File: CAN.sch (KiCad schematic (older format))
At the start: 2 parts

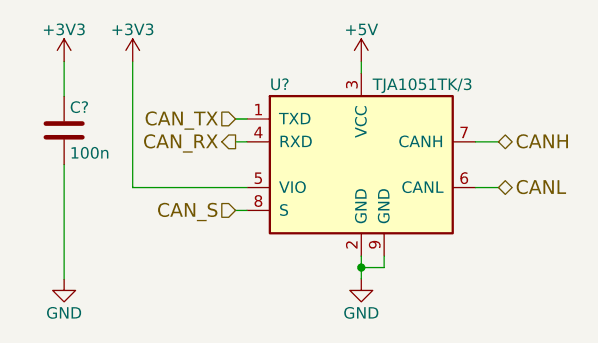
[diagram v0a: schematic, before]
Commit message: Finished schematic
Motordriver still needs footprint, it's necessary to choose new bulk capacitors
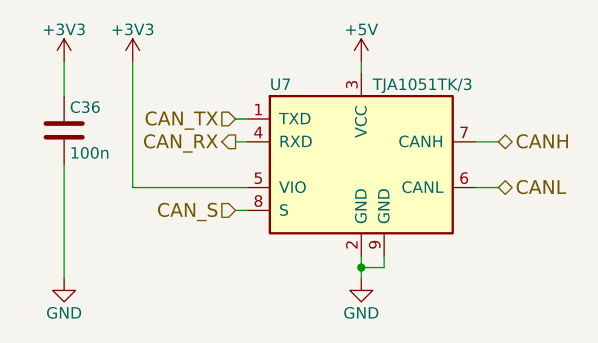
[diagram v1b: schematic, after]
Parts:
- C36: renamed from C?; footprint (none) -> Capacitors_SMD:C_0402
- gave numbers to parts that had none: 1
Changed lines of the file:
@@
 $EndDescr
 $Comp
-L TJA1051TK/3 U?
+L TJA1051TK/3 U7
 U 1 1 5A0B0C6C
 P 5900 4000
-F 0 "U?" H 5500 4350 50  0000 L CNN
+F 0 "U7" H 5500 4350 50  0000 L CNN
 F 1 "TJA1051TK/3" H 5950 4350 50  0000 L CNN
 F 2 "Housings_DFN_QFN:DFN-8-1EP_3x3mm_Pitch0.65mm" H 5900 3500 50  0001 C CIN
@@
 	5900 3550 5900 3600
 $Comp
-L GND #PWR?
+L GND #PWR85
 U 1 1 5A0B0CD3
 P 5900 4500
-F 0 "#PWR?" H 5900 4250 50  0001 C CNN
+F 0 "#PWR85" H 5900 4250 50  0001 C CNN
 F 1 "GND" H 5900 4350 50  0000 C CNN
 F 2 "" H 5900 4500 50  0001 C CNN
@@
 $EndComp
 Wire Wire Line
-	5900 4400 5900 4450
-Wire Wire Line
-	5900 4450 5900 4500
+	5900 4400 5900 4500
 Wire Wire Line
 	6000 4400 6000 4450
@@
 Connection ~ 5900 4450
 $Comp
-L +3V3 #PWR?
+L +3V3 #PWR83
 U 1 1 5A0B0CFF
 P 4900 3550
-F 0 "#PWR?" H 4900 3400 50  0001 C CNN
+F 0 "#PWR83" H 4900 3400 50  0001 C CNN
 F 1 "+3V3" H 4900 3690 50  0000 C CNN
 F 2 "" H 4900 3550 50  0001 C CNN
@@
 	5350 3800 5400 3800
 $Comp
-L C C?
+L C C36
 U 1 1 5A0B0D90
 P 4600 3850
-F 0 "C?" H 4625 3950 50  0000 L CNN
+F 0 "C36" H 4625 3950 50  0000 L CNN
 F 1 "100n" H 4625 3750 50  0000 L CNN
-F 2 "" H 4638 3700 50  0001 C CNN
+F 2 "Capacitors_SMD:C_0402" H 4638 3700 50  0001 C CNN
 F 3 "" H 4600 3850 50  0001 C CNN
 	1    4600 3850
@@
 $EndComp
 $Comp
-L +3V3 #PWR?
+L +3V3 #PWR81
 U 1 1 5A0B0DF3
 P 4600 3550
-F 0 "#PWR?" H 4600 3400 50  0001 C CNN
+F 0 "#PWR81" H 4600 3400 50  0001 C CNN
 F 1 "+3V3" H 4600 3690 50  0000 C CNN
 F 2 "" H 4600 3550 50  0001 C CNN
@@
 $EndComp
 $Comp
-L GND #PWR?
+L GND #PWR82
 U 1 1 5A0B0E04
 P 4600 4500
-F 0 "#PWR?" H 4600 4250 50  0001 C CNN
+F 0 "#PWR82" H 4600 4250 50  0001 C CNN
 F 1 "GND" H 4600 4350 50  0000 C CNN
 F 2 "" H 4600 4500 50  0001 C CNN
@@
 	4600 3550 4600 3700
 $Comp
-L +5V #PWR?
+L +5V #PWR84
 U 1 1 5A0B0E45
 P 5900 3550
-F 0 "#PWR?" H 5900 3400 50  0001 C CNN
+F 0 "#PWR84" H 5900 3400 50  0001 C CNN
 F 1 "+5V" H 5900 3690 50  0000 C CNN
 F 2 "" H 5900 3550 50  0001 C CNN

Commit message: udated schematics
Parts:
- C36: value 100n -> 100n 6V3
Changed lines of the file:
@@
 	5900 3550 5900 3600
 $Comp
-L GND #PWR087
+L GND #PWR89
 U 1 1 5A0B0CD3
 P 5900 4500
-F 0 "#PWR087" H 5900 4250 50  0001 C CNN
+F 0 "#PWR89" H 5900 4250 50  0001 C CNN
 F 1 "GND" H 5900 4350 50  0000 C CNN
 F 2 "" H 5900 4500 50  0001 C CNN
@@
 Connection ~ 5900 4450
 $Comp
-L +3V3 #PWR088
+L +3V3 #PWR87
 U 1 1 5A0B0CFF
 P 4900 3550
-F 0 "#PWR088" H 4900 3400 50  0001 C CNN
+F 0 "#PWR87" H 4900 3400 50  0001 C CNN
 F 1 "+3V3" H 4900 3690 50  0000 C CNN
 F 2 "" H 4900 3550 50  0001 C CNN
@@
 P 4600 3850
 F 0 "C36" H 4625 3950 50  0000 L CNN
-F 1 "100n" H 4625 3750 50  0000 L CNN
+F 1 "100n 6V3" V 4450 3700 50  0000 L CNN
 F 2 "Capacitors_SMD:C_0402" H 4638 3700 50  0001 C CNN
 F 3 "" H 4600 3850 50  0001 C CNN
@@
 $EndComp
 $Comp
-L +3V3 #PWR089
+L +3V3 #PWR85
 U 1 1 5A0B0DF3
 P 4600 3550
-F 0 "#PWR089" H 4600 3400 50  0001 C CNN
+F 0 "#PWR85" H 4600 3400 50  0001 C CNN
 F 1 "+3V3" H 4600 3690 50  0000 C CNN
 F 2 "" H 4600 3550 50  0001 C CNN
@@
 $EndComp
 $Comp
-L GND #PWR090
+L GND #PWR86
 U 1 1 5A0B0E04
 P 4600 4500
-F 0 "#PWR090" H 4600 4250 50  0001 C CNN
+F 0 "#PWR86" H 4600 4250 50  0001 C CNN
 F 1 "GND" H 4600 4350 50  0000 C CNN
 F 2 "" H 4600 4500 50  0001 C CNN
@@
 	4600 3550 4600 3700
 $Comp
-L +5V #PWR091
+L +5V #PWR88
 U 1 1 5A0B0E45
 P 5900 3550
-F 0 "#PWR091" H 5900 3400 50  0001 C CNN
+F 0 "#PWR88" H 5900 3400 50  0001 C CNN
 F 1 "+5V" H 5900 3690 50  0000 C CNN
 F 2 "" H 5900 3550 50  0001 C CNN

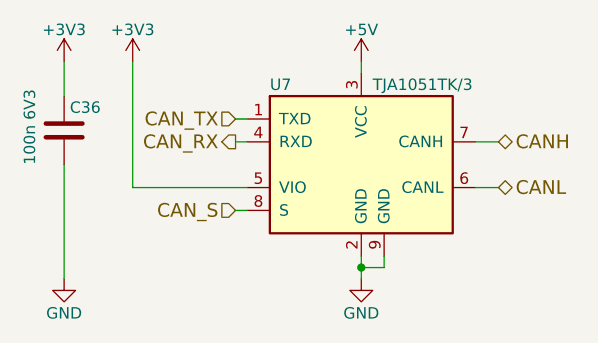
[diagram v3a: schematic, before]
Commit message: started modifying for 3 stepper motors
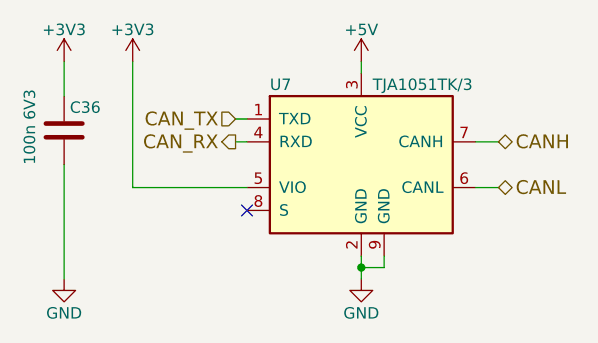
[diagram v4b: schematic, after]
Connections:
- net CAN_S: no longer names the net of U7.8 (S)
- no-connect marks 0 -> 1
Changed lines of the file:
@@
 $Descr A4 11693 8268
 encoding utf-8
-Sheet 4 4
+Sheet 2 4
 Title ""
 Date ""
@@
 Wire Wire Line
 	6400 4100 6500 4100
-Text HLabel 5350 4200 0    60   Input ~ 0
-CAN_S
-Wire Wire Line
-	5350 4200 5400 4200
 Text HLabel 5350 3900 0    60   Output ~ 0
 CAN_RX
@@
 	1    0    0    -1
 $EndComp
+NoConn ~ 5400 4200
 $EndSCHEMATC
